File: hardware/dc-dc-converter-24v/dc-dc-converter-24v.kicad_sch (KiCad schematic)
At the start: 56 parts, among them J1 12V, J2 24V, Q1 SQJA42EP, Q2 SQJA42EP, Q3 SQJA42EP, Q4 SQJA42EP, U1 LM5176

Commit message: start with redesign of DC-DC converter
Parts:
- removed C10, C14, C15, C3, C5, C7: 100nF, benediktibk:C_0603_1608Metric_Pad1.08x0.95mm_HandSolder, symbol benediktibk:C_100nF_SMD_0603_50V
- removed C11: 560pF, benediktibk:C_0603_1608Metric_Pad1.08x0.95mm_HandSolder, symbol benediktibk:C_560pF_SMD_0603_50V_5%
- removed C12: 240pF, benediktibk:C_0805_2012Metric_Pad1.18x1.45mm_HandSolder, symbol benediktibk:C_240pF_SMD_0805_250V_10%
- removed C13: 33nF, benediktibk:C_0603_1608Metric_Pad1.08x0.95mm_HandSolder, symbol benediktibk:C_33nF_SMD_0603_50V_10%
- removed C16: 47pF, benediktibk:C_0603_1608Metric_Pad1.08x0.95mm_HandSolder, symbol benediktibk:C_47pF_SMD_0603_100V_5%
- removed C9: 1uF, benediktibk:C_0603_1608Metric_Pad1.08x0.95mm_HandSolder, symbol benediktibk:C_1uF_SMD_0603_50V_10%
- removed D2: Vout good, benediktibk:D_0603_1608Metric_Pad1.05x0.95mm_HandSolder, symbol benediktibk:LED_green_0603
- removed D4, D5: BAT54WS, benediktibk:D_SOD-323, symbol benediktibk:BAT54WS
- removed L1: 2.5µH, benediktibk:ETQP8, symbol benediktibk:L_2_5µH_30A
- removed Q3, Q4: SQJA42EP, benediktibk:SQJA42EPT1_GE3, symbol benediktibk:SQJA42EP
- removed R10: 10Ohm, benediktibk:R_0603_1608Metric_Pad0.98x0.95mm_HandSolder, symbol benediktibk:R_10Ohm_SMD_0603_100mW_1%
- removed R11, R12, R3: 10kOhm, benediktibk:R_0603_1608Metric_Pad0.98x0.95mm_HandSolder, symbol benediktibk:R_10kOhm_SMD_0603_100mW_1%
- removed R13: 20kOhm, benediktibk:R_0603_1608Metric_Pad0.98x0.95mm_HandSolder, symbol benediktibk:R_20kOhm_SMD_0603_100mW_1%
- removed R14: 270kOhm, benediktibk:R_0603_1608Metric_Pad0.98x0.95mm_HandSolder, symbol benediktibk:R_270kOhm_SMD_0603_100mW_1%
- removed R15, R16: 100Ohm, benediktibk:R_0603_1608Metric_Pad0.98x0.95mm_HandSolder, symbol benediktibk:R_100Ohm_SMD_0603_100mW_1%
- removed R17: 4mOhm, benediktibk:R_2512_6332Metric_Pad1.40x3.35mm_HandSolder, symbol benediktibk:R_4mOhm_SMD_2512_2W_1%
- removed R2: 1kOhm, benediktibk:R_0603_1608Metric_Pad0.98x0.95mm_HandSolder, symbol benediktibk:R_1kOhm_SMD_0603_100mW_1%
- removed R4: 24kOhm, benediktibk:R_0603_1608Metric_Pad0.98x0.95mm_HandSolder, symbol benediktibk:R_24kOhm_SMD_0603_100mW_1%
- removed R5: 93.1kOhm, benediktibk:R_0603_1608Metric_Pad0.98x0.95mm_HandSolder, symbol benediktibk:R_93_1kOhm_SMD_0603_100mW_0_1%
- removed R6: 220kOhm, benediktibk:R_0603_1608Metric_Pad0.98x0.95mm_HandSolder, symbol benediktibk:R_220kOhm_SMD_0603_100mW_1%
- removed R7: 43kOhm, benediktibk:R_0603_1608Metric_Pad0.98x0.95mm_HandSolder, symbol benediktibk:R_43kOhm_SMD_0603_100mW_1%
- removed R8: 0Ohm, benediktibk:R_0603_1608Metric_Pad0.98x0.95mm_HandSolder, symbol benediktibk:R_0Ohm_SMD_0603_100mW_0%
- removed R9: 2kOhm, benediktibk:R_0603_1608Metric_Pad0.98x0.95mm_HandSolder, symbol benediktibk:R_2kOhm_SMD_0603_100mW_1%
- removed U1: LM5176, benediktibk:LM5176, symbol benediktibk:LM5176
- added IC1: LM5122MHX_NOPB, benediktibk:SOP65P640X110-21N, symbol benediktibk:LM5122MHX_NOPB
- added L1: 7443641000B, benediktibk:7443641000B, symbol benediktibk:7443641000B
- added R2: R_2mOhm_SMD_2512_5W_1%, benediktibk:R_2512_6332Metric_Pad1.40x3.35mm_HandSolder, symbol benediktibk:R_2mOhm_SMD_2512_5W_1%
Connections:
- net GND: now also Q2.1 (S), IC1.15 (PGND), IC1.2 (OPT), IC1.21 (EP), IC1.9 (AGND), L1.3
- net Vin: no longer D3.2 (A), Q1.3 (D)
- net Vout: now also Q1.3 (D)
- net at Q1.1 (S), Q2.3 (D): now also L1.1
- net at Q2.2 (G): now also IC1.16 (LO)
- new net: L1.2, R2.2
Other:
- moved on the sheet: D3, Q1, Q2

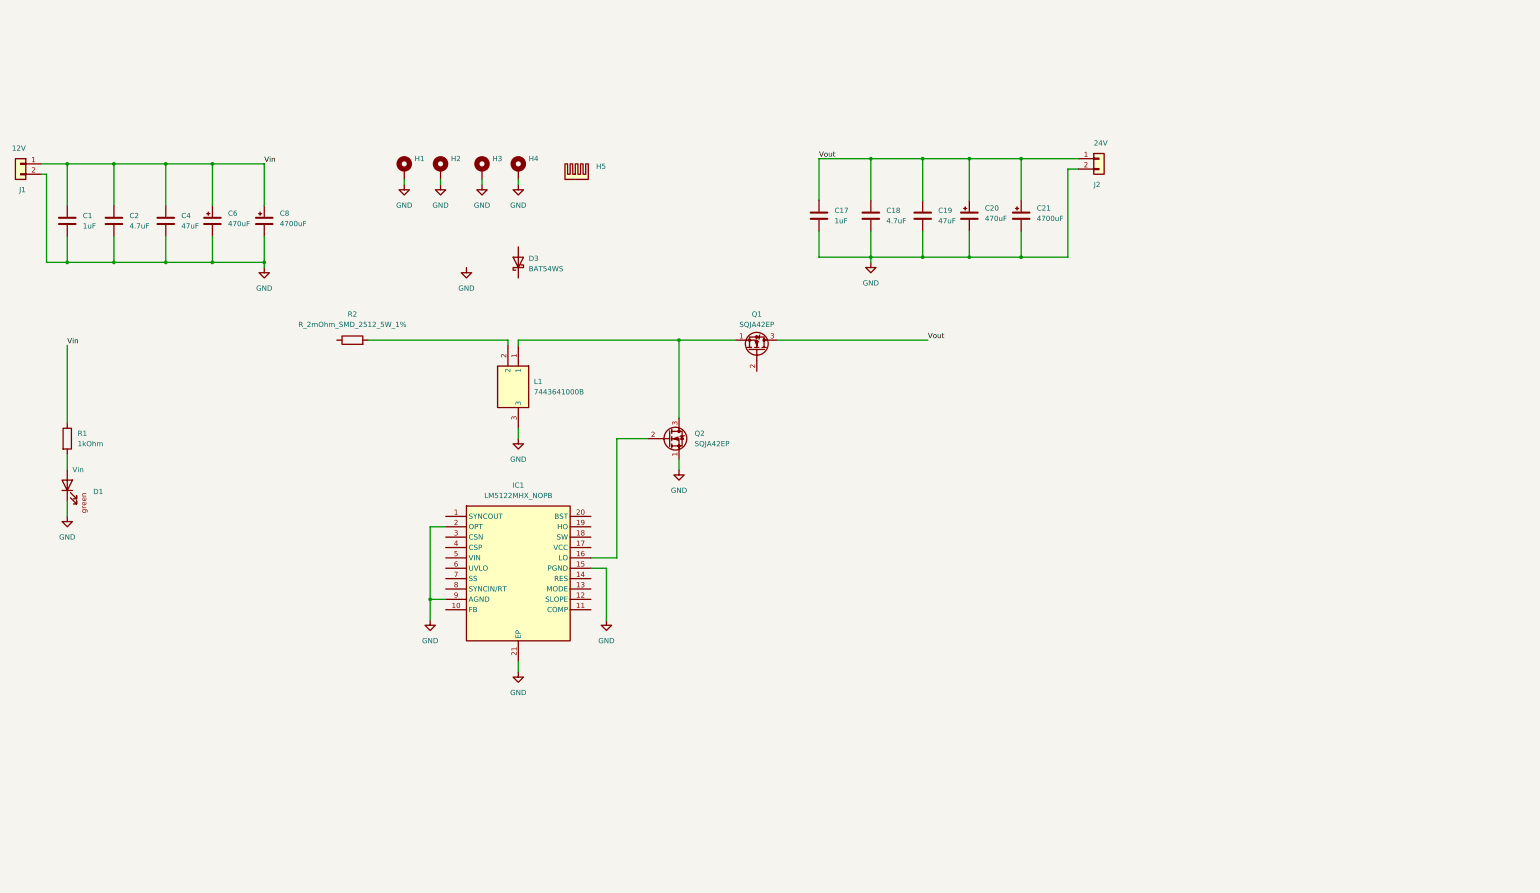
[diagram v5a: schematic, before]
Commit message: finish redesign of schematic of DC-DC converter
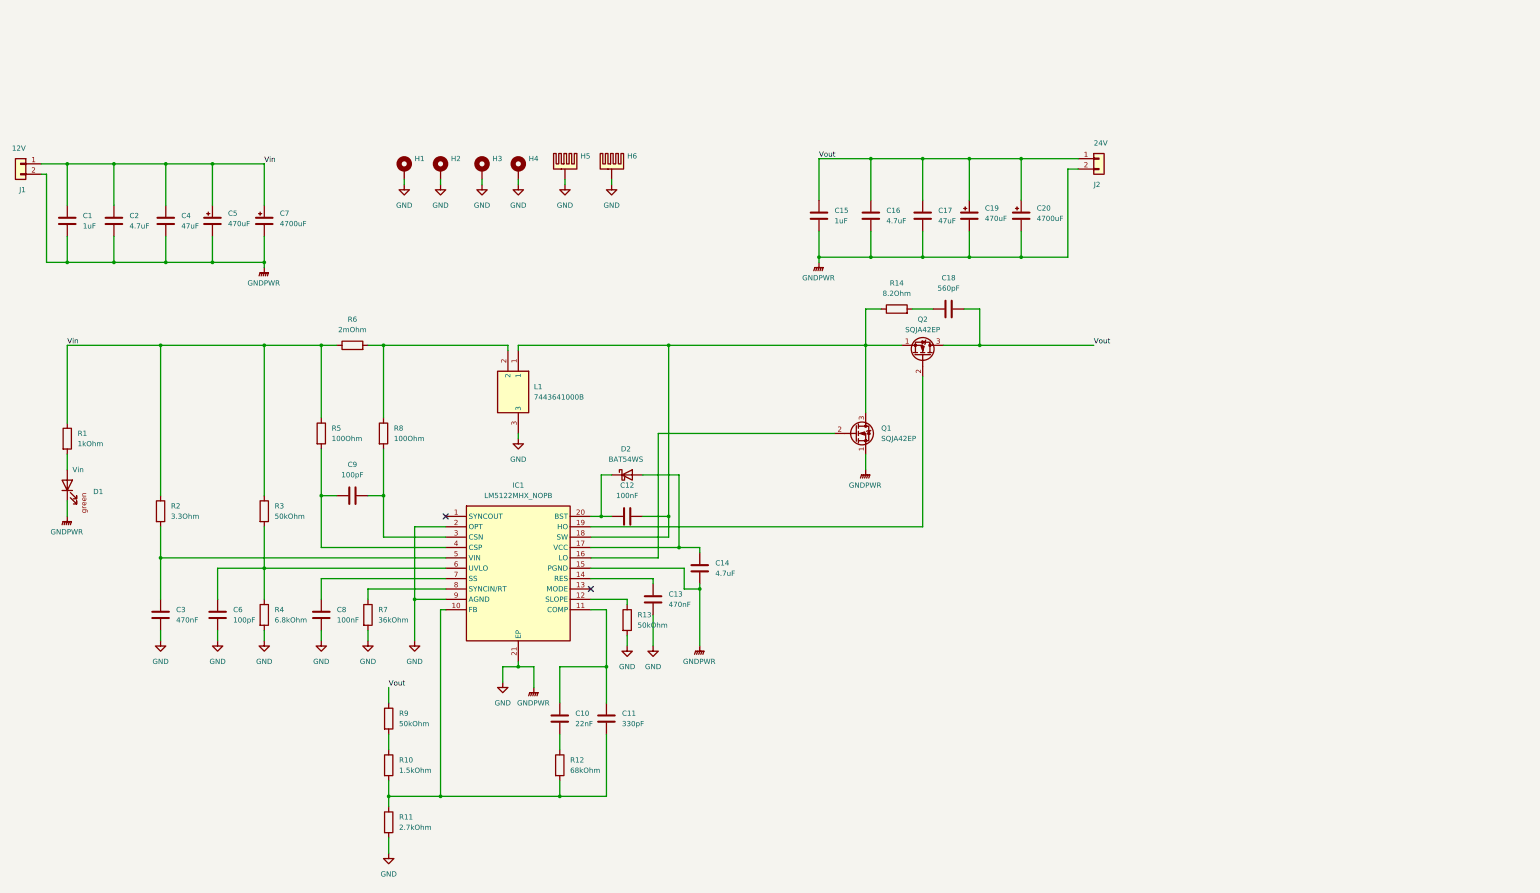
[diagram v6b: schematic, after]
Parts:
- removed D3: BAT54WS, benediktibk:D_SOD-323, symbol benediktibk:BAT54WS
- removed H5: heatsink_ATS-CPX045045035-164-C2-R0, benediktibk:heatsink_984-CPX04504-164C2R0, symbol benediktibk:heatsink_ATS-CPX045045035-164-C2-R0
- added C10: 22nF, benediktibk:C_0603_1608Metric_Pad1.08x0.95mm_HandSolder, symbol benediktibk:C_22nF_SMD_0603_16V_10%
- added C11: 330pF, benediktibk:C_0603_1608Metric_Pad1.08x0.95mm_HandSolder, symbol benediktibk:C_330pF_SMD_0603_50V_5%
- added C12, C8: 100nF, benediktibk:C_0603_1608Metric_Pad1.08x0.95mm_HandSolder, symbol benediktibk:C_100nF_SMD_0603_50V
- added C13, C3: 470nF, benediktibk:C_0603_1608Metric_Pad1.08x0.95mm_HandSolder, symbol benediktibk:C_470nF_SMD_0603_16V
- added C14: 4.7uF, benediktibk:C_0805_2012Metric_Pad1.18x1.45mm_HandSolder, symbol benediktibk:C_4_7uF_SMD_0805_50V_10%
- added C18: 560pF, benediktibk:C_0603_1608Metric_Pad1.08x0.95mm_HandSolder, symbol benediktibk:C_560pF_SMD_0603_50V_5%
- added C6, C9: 100pF, benediktibk:C_0603_1608Metric_Pad1.08x0.95mm_HandSolder, symbol benediktibk:C_100pF_SMD_0603_50V_10%
- added D2: BAT54WS, benediktibk:D_SOD-323, symbol benediktibk:BAT54WS
- added H5, H6: heatsink_HSB43-454515P, benediktibk:HSB43-454515P, symbol benediktibk:heatsink_HSB43-454515P
- added R10: 1.5kOhm, benediktibk:R_0603_1608Metric_Pad0.98x0.95mm_HandSolder, symbol benediktibk:R_1_5kOhm_SMD_0603_100mW_0_1%
- added R11: 2.7kOhm, benediktibk:R_0603_1608Metric_Pad0.98x0.95mm_HandSolder, symbol benediktibk:R_2_7kOhm_SMD_0603_100mW_0_1%
- added R12: 68kOhm, benediktibk:R_0603_1608Metric_Pad0.98x0.95mm_HandSolder, symbol benediktibk:R_68kOhm_SMD_0603_100mW_1%
- added R13, R3, R9: 50kOhm, benediktibk:R_0603_1608Metric_Pad0.98x0.95mm_HandSolder, symbol benediktibk:R_50kOhm_SMD_0603_100mW_0_1%
- added R14: 8.2Ohm, benediktibk:R_0603_1608Metric_Pad0.98x0.95mm_HandSolder, symbol benediktibk:R_8_2Ohm_SMD_0603_125mW_5%
- added R2: 3.3Ohm, benediktibk:R_0603_1608Metric_Pad0.98x0.95mm_HandSolder, symbol benediktibk:R_3_3Ohm_SMD_0603_100mW_0_1%
- added R4: 6.8kOhm, benediktibk:R_0603_1608Metric_Pad0.98x0.95mm_HandSolder, symbol benediktibk:R_6_8kOhm_SMD_0603_210mW_0_1%
- added R5, R8: 100Ohm, benediktibk:R_0603_1608Metric_Pad0.98x0.95mm_HandSolder, symbol benediktibk:R_100Ohm_SMD_0603_100mW_1%
- added R7: 36kOhm, benediktibk:R_0603_1608Metric_Pad0.98x0.95mm_HandSolder, symbol benediktibk:R_36kOhm_SMD_0603_100mW_1%
- R6: renamed from R2; value R_2mOhm_SMD_2512_5W_1% -> 2mOhm
- renumbered C17 to C15, C18 to C16, C19 to C17, C20 to C19, C21 to C20, C6 to C5, C8 to C7, Q2 to Q1, Q1 to Q2
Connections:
- net GND: now also C13.2, C14.2, C3.2, C6.2, C8.2, H5.PAD, H6.PAD, R11.2, R13.2, R4.2, R7.2
- net Vin: now also R6.1, R2.1, R3.1, R5.1
- net Vout: now also C18.2, R9.1
- net at L1.1, Q1.3 (D), Q2.1 (S): now also IC1.18 (SW), C12.2, R14.1
- net at L1.2, R6.2: now also R8.1
- net at IC1.10 (FB): now also C11.2, R10.2, R11.1, R12.2
- net at IC1.11 (COMP): now also C10.1, C11.1
- net at IC1.12 (SLOPE): now also R13.1
- net at IC1.14 (RES): now also C13.1
- net at IC1.17 (VCC): now also C14.1, D2.2 (A)
- net at IC1.19 (HO): now also Q2.2 (G)
- net at IC1.20 (BST): now also C12.1, D2.1 (K)
- net at IC1.3 (CSN): now also C9.2, R8.2
- net at IC1.4 (CSP): now also C9.1, R5.2
- net at IC1.5 (VIN): now also C3.1, R2.2
- net at IC1.6 (UVLO): now also C6.1, R3.2, R4.1
- net at IC1.7 (SS): now also C8.1
- net at IC1.8 (SYNCIN/RT): now also R7.1
- new net: C10.2, R12.1
- new net: C18.1, R14.2
- new net: R10.1, R9.2
- no-connect marks 0 -> 2
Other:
- moved on the sheet: L1, Q1, Q2, R6

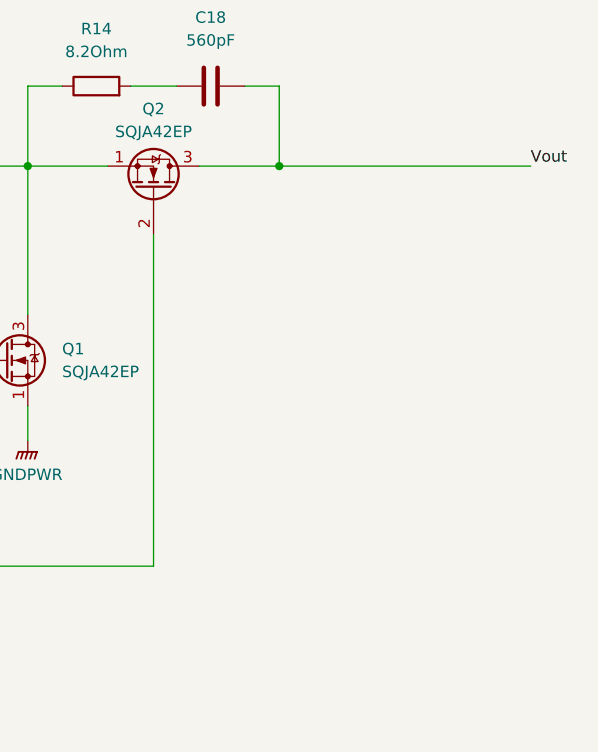
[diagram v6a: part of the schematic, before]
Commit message: create layout for DC-DC converter
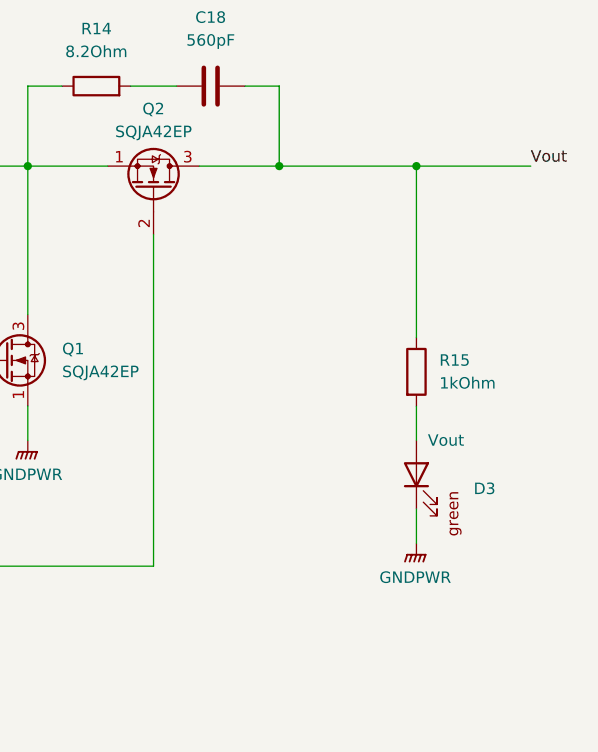
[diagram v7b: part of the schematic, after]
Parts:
- added D3: Vout, benediktibk:D_0603_1608Metric_Pad1.05x0.95mm_HandSolder, symbol benediktibk:LED_green_0603
- added R15: 1kOhm, benediktibk:R_0603_1608Metric_Pad0.98x0.95mm_HandSolder, symbol benediktibk:R_1kOhm_SMD_0603_100mW_1%
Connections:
- net GND: now also D3.1 (K)
- net Vout: now also R15.1
- new net: D3.2 (A), R15.2

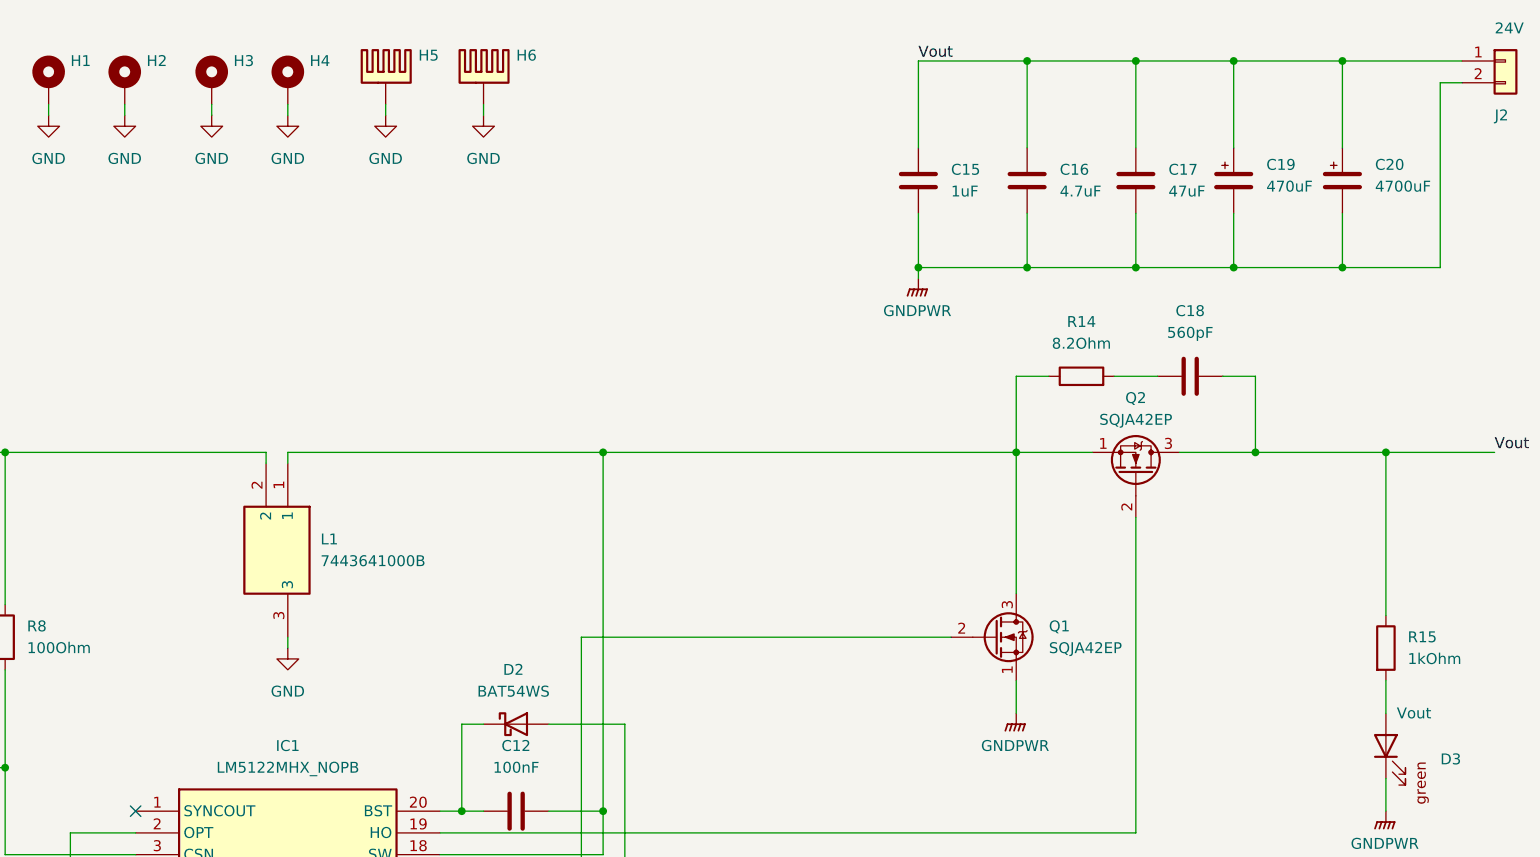
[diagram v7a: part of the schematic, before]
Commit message: improve cooling for DC-DC converter
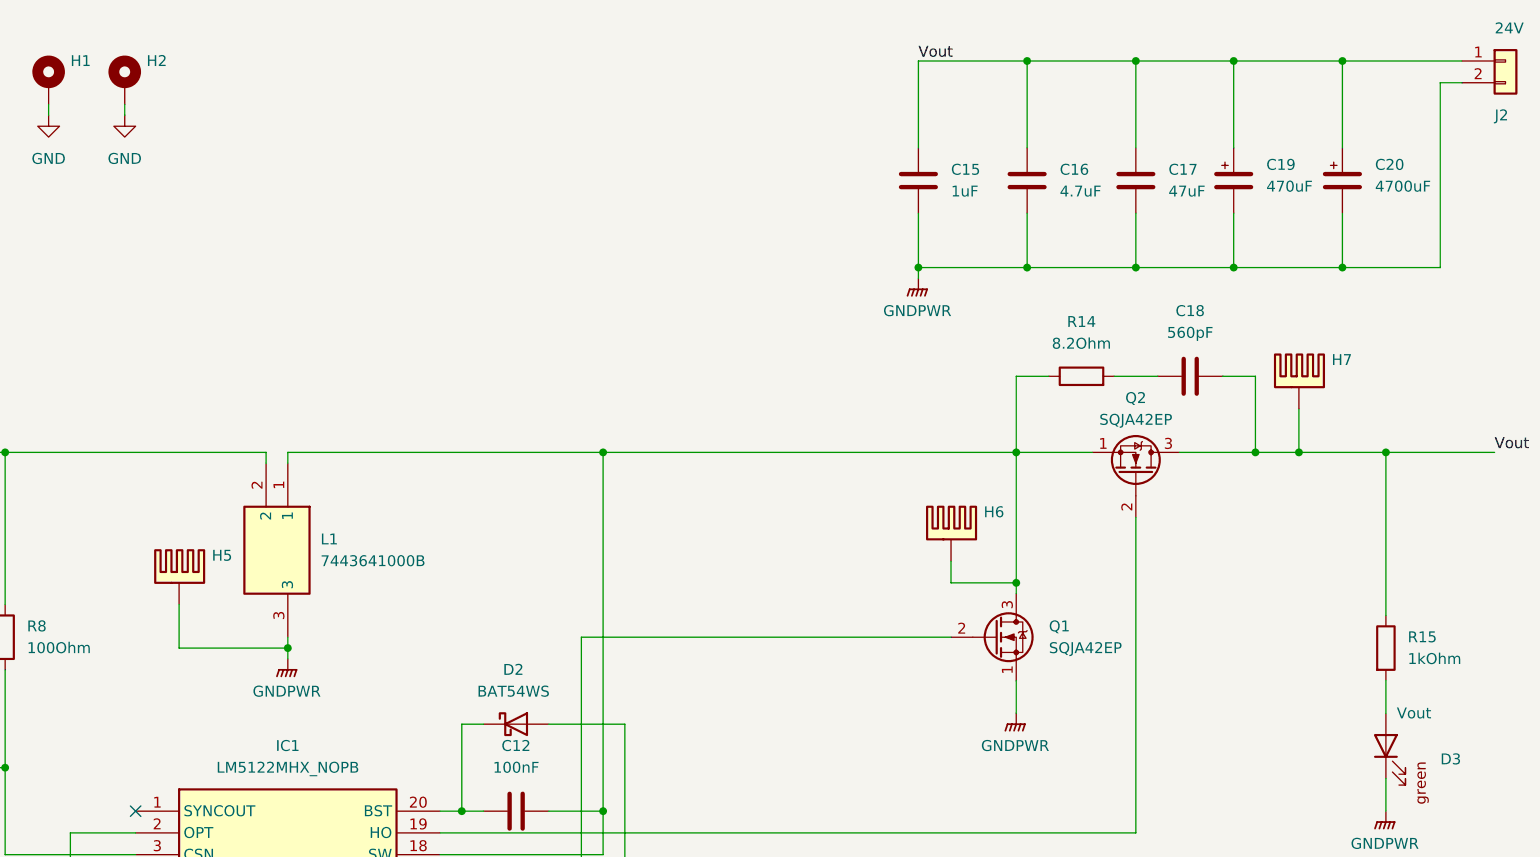
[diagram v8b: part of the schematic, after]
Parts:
- removed H3, H4: MountingHole_Pad_M6, benediktibk:MountingHole_6.4mm_M6_Pad_TopBottom, symbol benediktibk:MountingHole_Pad_M6
- added H7: heatsink_HSB43-454515P, benediktibk:HSB43-454515P, symbol benediktibk:heatsink_HSB43-454515P
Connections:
- net GND: no longer H6.PAD
- net Vout: now also H7.PAD
- net at C12.2, IC1.18 (SW), L1.1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: now also H6.PAD
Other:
- moved on the sheet: H5, H6
